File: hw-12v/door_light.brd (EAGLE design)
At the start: 26.2 x 27.6 mm, 24 parts, among them IC1 TINY13-20SSU, IC2 78L05F, T1 IRFML8244, T2 IRFML8244, T3 KP-3216P3C

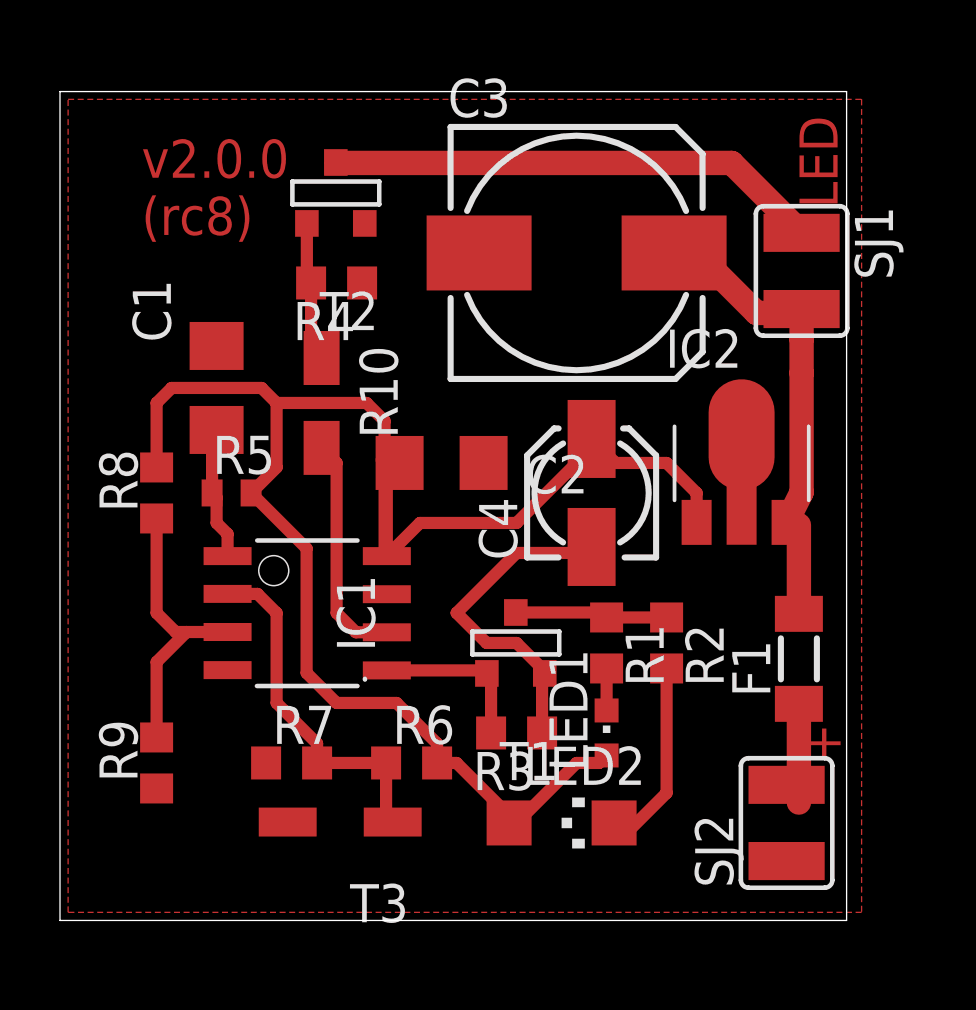
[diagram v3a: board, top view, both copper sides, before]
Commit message: fixed R5 size (was 40x should be 603)
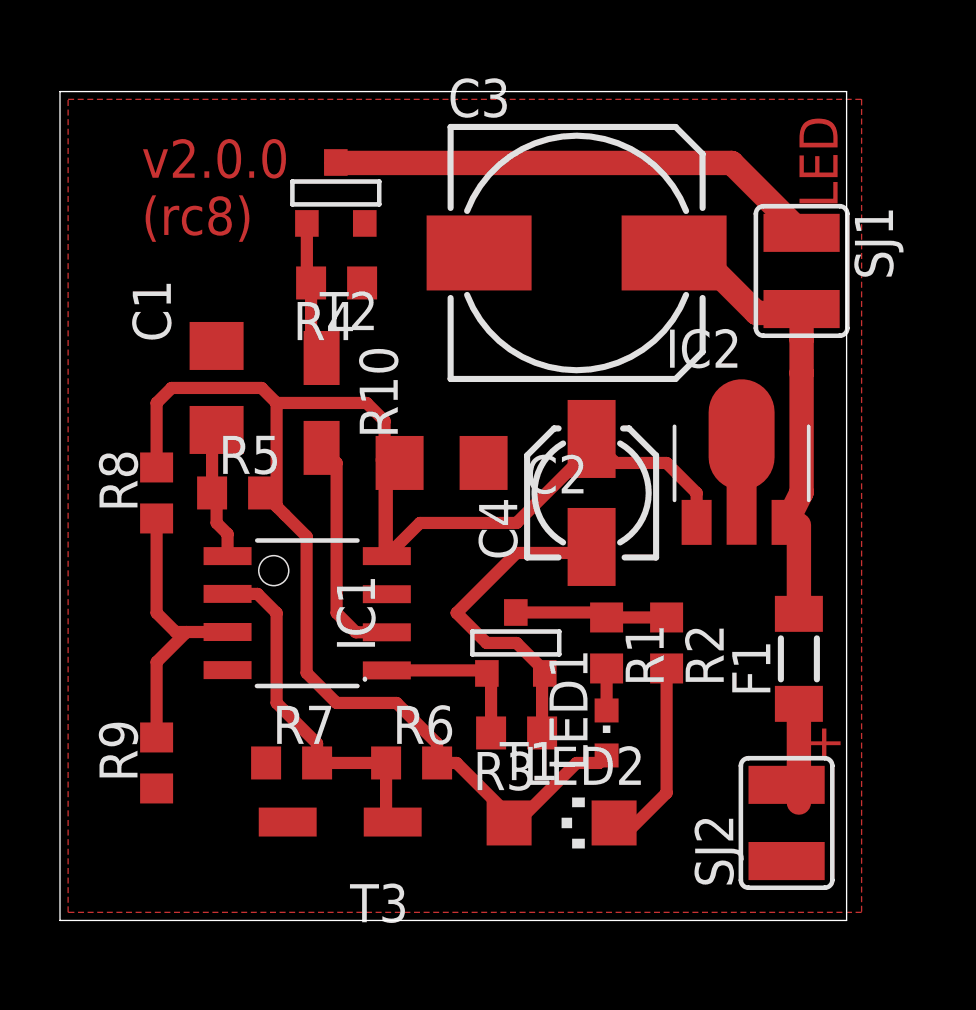
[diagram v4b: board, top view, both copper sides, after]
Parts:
- R5: device rcl:R0402 -> rcl:R0603
- moved R5 0.20 mm to (28.7, 56.0)
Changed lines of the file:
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@@
 </element>
 <element name="F1" library="rcl" package="MINI_MELF-0204W" value="F750mA" x="47.41" y="50.47" rot="R90"/>
-<element name="R5" library="rcl" package="R0402" value="10kR" x="28.5" y="56"/>
+<element name="R5" library="rcl" package="R0603" value="10kR" x="28.7" y="56"/>
 <element name="R7" library="rcl" package="R0603" value="2.7kR" x="30.5" y="47"/>
 <element name="R8" library="rcl" package="R0603" value="10kR" x="26" y="56" rot="R90"/>
@@
 <contactref element="IC1" pad="1"/>
 <contactref element="R5" pad="1"/>
+<wire x1="28.366" y1="53.895" x2="28.366" y2="54.634" width="0.4064" layer="1"/>
+<wire x1="28.366" y1="54.634" x2="28" y2="55" width="0.4064" layer="1"/>
 <wire x1="27.85" y1="56" x2="27.85" y2="57.95" width="0.4064" layer="1"/>
 <wire x1="27.85" y1="57.95" x2="28" y2="58.1" width="0.4064" layer="1"/>
-<wire x1="28.366" y1="53.895" x2="28.366" y2="54.634" width="0.4064" layer="1"/>
-<wire x1="28.366" y1="54.634" x2="28" y2="55" width="0.4064" layer="1"/>
 <wire x1="28" y1="55" x2="28" y2="55.85" width="0.4064" layer="1"/>
 <wire x1="28" y1="55.85" x2="27.85" y2="56" width="0.4064" layer="1"/>
@@
 <contactref element="IC2" pad="1"/>
 <contactref element="C4" pad="+"/>
-<wire x1="31" y1="50" x2="31" y2="54.15" width="0.4064" layer="1"/>
+<wire x1="31" y1="50" x2="31" y2="54.55" width="0.4064" layer="1"/>
 <wire x1="26.5" y1="59.5" x2="29.5" y2="59.5" width="0.4064" layer="1"/>
-<wire x1="30" y1="59" x2="30" y2="56.85" width="0.4064" layer="1"/>
-<wire x1="30" y1="56.85" x2="29.15" y2="56" width="0.4064" layer="1"/>
+<wire x1="30" y1="59" x2="30" y2="55.55" width="0.4064" layer="1"/>
 <wire x1="29.5" y1="59.5" x2="30" y2="59" width="0.4064" layer="1"/>
 <wire x1="26.5" y1="59.5" x2="26" y2="59" width="0.4064" layer="1"/>
@@
 <wire x1="34.1" y1="57" x2="33.6" y2="56.4" width="0.4064" layer="1"/>
 <wire x1="34.779" y1="55" x2="38" y2="55" width="0.4064" layer="1"/>
-<wire x1="31" y1="54.15" x2="29.15" y2="56" width="0.4064" layer="1"/>
 <wire x1="33.674" y1="53.895" x2="33.674" y2="56.326" width="0.4064" layer="1"/>
 <wire x1="33.674" y1="56.326" x2="33.6" y2="56.4" width="0.4064" layer="1"/>
@@
 <wire x1="43" y1="57" x2="41.3" y2="57" width="0.4064" layer="1"/>
 <wire x1="41.3" y1="57" x2="40.5" y2="57.8" width="0.4064" layer="1"/>
+<wire x1="31" y1="54.55" x2="30.275" y2="55.275" width="0.4064" layer="1"/>
+<wire x1="30" y1="55.55" x2="29.55" y2="56" width="0.4064" layer="1"/>
+<wire x1="30" y1="55.55" x2="30.275" y2="55.275" width="0.4064" layer="1"/>
 </signal>
 <signal name="+12V">

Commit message: fuse changed from 750mA to 350mA
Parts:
- F1: value F750mA -> F350mA
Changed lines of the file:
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@@
 <attribute name="VALUE" x="26.984" y="55.944" size="1.27" layer="27" ratio="10" rot="R90"/>
 </element>
-<element name="F1" library="rcl" package="MINI_MELF-0204W" value="F750mA" x="47.41" y="50.47" rot="R90"/>
+<element name="F1" library="rcl" package="MINI_MELF-0204W" value="F350mA" x="47.41" y="50.47" rot="R90"/>
 <element name="R5" library="rcl" package="R0603" value="10kR" x="28.7" y="56"/>
 <element name="R7" library="rcl" package="R0603" value="2.7kR" x="30.5" y="47"/>
